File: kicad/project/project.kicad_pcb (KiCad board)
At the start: 2 copper layers, 42 parts, among them J1 SWD, J2 UART, U1 ADS1015, U2 AP7380, U3 STM32L031F4Px, U4 VN7003ALH

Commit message: Placing parts
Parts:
- R1, R2, R7: moved to B.Cu
- moved U1 83.7 mm to (179.1, 102.9), turned to 180 degrees
- moved C6 76.3 mm to (74.9, 60.0)
- moved C4 76.3 mm to (80.7, 52.8)
- moved C5 76.3 mm to (75.3, 58.0)
- moved C7 76.3 mm to (80.7, 54.3)
- moved C8 76.3 mm to (88.3, 45.7)
- moved R11 76.3 mm to (91.7, 48.7)
- moved R12 76.3 mm to (80.7, 55.8)
- moved R13 76.3 mm to (82.0, 57.4)
- moved R16 76.3 mm to (71.7, 58.2)
- moved R3 76.3 mm to (95.0, 45.7)
- moved R4 76.3 mm to (84.0, 52.8)
- moved R5 76.3 mm to (78.6, 58.0)
- moved R6 76.3 mm to (84.0, 54.3)
- moved TP1 76.3 mm to (39.8, 53.4)
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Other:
- board outline added: 70 x 70 mm

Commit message: Panel mount meter
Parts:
- added MES1: Voltmeter, Connector_PinHeader_2.54mm:PinHeader_2x01_P2.54mm_Vertical, F.Cu at (90.1, 79.7)
- added MES2: Amperemeter, Connector_PinHeader_2.54mm:PinHeader_2x01_P2.54mm_Vertical, F.Cu at (97.7, 79.7)
- BT1, D1, D2, D3, D4, SC1: moved to B.Cu
- R1, R2, R7: moved to F.Cu
- U4: footprint theapi:Octapak -> Package_TO_SOT_SMD:Infineon_PG-TO-220-7Lead_TabPin8
- moved U1 82.5 mm to (108.0, 61.0)
- moved D5 81.5 mm to (97.5, 121.0), turned to 270 degrees
- moved BT1 77.4 mm to (97.5, 108.0), turned to 270 degrees
- moved R14 67.1 mm to (104.6, 121.6), turned to 270 degrees
- moved R10 61.1 mm to (107.6, 121.6), turned to 90 degrees
- moved C9 61.0 mm to (107.6, 117.4), turned to 90 degrees
- moved R17 59.0 mm to (108.5, 87.5), turned to 0 degrees
- moved D4 55.4 mm to (108.4, 87.6), turned to 180 degrees
- moved R15 55.1 mm to (110.6, 121.6), turned to 90 degrees
- moved D3 52.6 mm to (108.4, 83.8), turned to 180 degrees
- moved R7 52.6 mm to (108.4, 83.8), turned to 0 degrees
- moved SC1 47.8 mm to (178.0, 113.0), turned to 90 degrees
- moved C11 32.8 mm to (172.5, 116.0)
- moved C1 27.8 mm to (153.1, 116.0), turned to 90 degrees
- moved C10 26.8 mm to (169.5, 116.0)
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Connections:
- BT1 pad 1: /BATT -> Net-(BT1-Pad1)
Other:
- board size 70 x 70 mm -> 95 x 60 mm
- board text added: "CHARGE CONTROLLER"

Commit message: Components placed
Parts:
- removed J2: UART, Connector_PinHeader_2.54mm:PinHeader_1x03_P2.54mm_Vertical
- removed MES1: Voltmeter, Connector_PinHeader_2.54mm:PinHeader_2x01_P2.54mm_Vertical
- removed MES2: Amperemeter, Connector_PinHeader_2.54mm:PinHeader_2x01_P2.54mm_Vertical
- added J3: Voltmeter, Connector_PinHeader_2.54mm:PinHeader_1x02_P2.54mm_Vertical_SMD_Pin1Left, F.Cu at (108.5, 110.0)
- BT1: value Battery -> Battery_Meter; footprint TerminalBlock:TerminalBlock_bornier-2_P5.08mm -> theapi:TerminalBlock_Meter
- D5, U3: moved to B.Cu
- TP1: footprint TestPoint:TestPoint_Pad_2.0x2.0mm -> TestPoint:TestPoint_Pad_D1.0mm
- U4: footprint Package_TO_SOT_SMD:Infineon_PG-TO-220-7Lead_TabPin8 -> theapi:Octapak; moved to B.Cu
- moved TP1 114.9 mm to (122.5, 133.0)
- moved C5 110.7 mm to (163.5, 124.9), turned to 90 degrees
- moved C8 98.9 mm to (144.6, 127.0)
- moved C4 98.3 mm to (137.5, 133.0)
- moved C7 93.7 mm to (138.5, 128.0), turned to 270 degrees
- moved R3 92.7 mm to (144.6, 124.0)
- moved C6 91.8 mm to (136.5, 128.0), turned to 270 degrees
- moved R11 89.2 mm to (130.6, 129.0)
- moved R12 86.1 mm to (130.6, 126.0)
- moved R13 81.7 mm to (130.6, 123.0)
- moved R6 81.5 mm to (108.6, 132.0)
- moved C2 78.8 mm to (122.8, 128.0)
- moved R4 77.2 mm to (108.6, 126.0)
- moved R5 77.0 mm to (108.6, 129.0)
- moved R16 69.1 mm to (123.5, 104.0), turned to 90 degrees
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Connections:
- BT1 pad 1: Net-(BT1-Pad1) -> /BATT
- U3 pad 9: UART_RX -> Net-(U3-Pad9)
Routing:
- net Net-(D5-Pad2): track 0.00 -> 73.4 mm
- net /BATT: track 0.00 -> 20.7 mm
- net +24V: track 0.00 -> 15.5 mm
- net -BATT: track 0.00 -> 6.03 mm
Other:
- board size 95 x 60 mm -> 98 x 60 mm
- board text removed: "CHARGE CONTROLLER"

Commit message: Main power traces
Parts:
- J1: moved to B.Cu
- moved J1 77.9 mm to (107.1, 132.0), turned to 270 degrees
- moved C2 46.0 mm to (168.8, 127.0)
- moved R4 46.0 mm to (154.6, 125.0)
- moved R5 46.0 mm to (154.6, 128.0)
- moved R6 46.0 mm to (154.6, 131.0)
- moved TP1 46.0 mm to (168.5, 132.0)
- moved U1 46.0 mm to (162.5, 127.0)
- moved C1 28.3 mm to (148.8, 119.1)
- moved C3 28.3 mm to (145.8, 119.1)
- moved C4 27.2 mm to (113.6, 120.0)
- moved U2 27.1 mm to (141.5, 122.5), turned to 270 degrees
- moved C6 24.2 mm to (112.5, 125.0)
- moved C7 24.2 mm to (114.5, 125.0)
- moved C8 24.2 mm to (120.6, 124.0)
- moved R11 24.2 mm to (106.6, 126.0)
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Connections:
- net Net-(D5-Pad2) renamed /OUT
- net Net-(R11-Pad1) renamed /INPUT
- R12 pad 1: Net-(R12-Pad1) -> /FR_DIAG
- R12 pad 2: /FR_DIAG -> Net-(R12-Pad2)
- U3 pad 12: /FR_DIAG -> Net-(R12-Pad2)
- U4 pad 6: Net-(R12-Pad1) -> /FR_DIAG
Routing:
- net /OUT: track 73.4 -> 20.8 mm
- net /BATT: track 20.7 -> 0.00 mm
- net -BATT: track 6.03 -> 0.00 mm
- net +24V: track 15.5 -> 14.1 mm, vias 0 -> 27
- added copper zone on B.Cu, net +24V
- added copper zone on F.Cu, net +24V
- added copper zone on B.Cu, net /BATT
- added copper zone on B.Cu, net /OUT

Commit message: Connections
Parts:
- R11, R12, R13: moved to B.Cu
- moved C4 56.1 mm to (169.7, 121.7)
- moved C6 56.1 mm to (168.6, 126.7)
- moved C7 56.1 mm to (170.6, 126.7)
- moved C8 56.1 mm to (176.7, 125.7)
- moved R3 56.1 mm to (176.7, 122.7)
- moved U3 56.1 mm to (169.6, 125.7)
- moved C2 54.7 mm to (114.0, 127.3), turned to 180 degrees
- moved TP1 49.3 mm to (119.4, 127.5)
- moved U1 48.5 mm to (114.1, 123.4)
- moved J1 42.4 mm to (149.5, 131.0)
- moved R6 37.7 mm to (118.8, 119.4), turned to 270 degrees
- moved R5 34.0 mm to (121.8, 119.4), turned to 270 degrees
- moved R11 31.1 mm to (137.7, 127.7)
- moved R12 31.1 mm to (137.7, 124.7)
- moved R13 31.1 mm to (137.7, 121.7)
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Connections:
- net /LED renamed /LED_1
- net /OUT renamed /LED_4
- net /PA4 renamed /LED_3
- net Net-(R2-Pad2) renamed /LED_2
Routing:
- net +3V3: track 0.00 -> 121.6 mm, vias 0 -> 2
- net /BATT_SENSE: track 0.00 -> 111.9 mm, vias 0 -> 1
- net /LED_3: track 0.00 -> 110.7 mm, vias 0 -> 1
- net /PANEL_SENSE: track 0.00 -> 102.7 mm, vias 0 -> 1
- net ADC_RDY: track 0.00 -> 68.4 mm, vias 0 -> 3
- net SDA: track 0.00 -> 64.2 mm, vias 0 -> 4
- net SCL: track 0.00 -> 62.8 mm, vias 0 -> 3
- net /LED_2: track 0.00 -> 59.9 mm, vias 0 -> 1
- net CURRENT_SENSE: track 0.00 -> 56.0 mm, vias 0 -> 1
- net +24V: track 14.1 -> 67.3 mm
- net /LED_1: track 0.00 -> 49.4 mm, vias 0 -> 1
- net GND: track 0.00 -> 46.8 mm, vias 0 -> 1
- net /FR_DIAG: track 0.00 -> 32.1 mm, vias 0 -> 2
- net Net-(R12-Pad2): track 0.00 -> 29.4 mm
- net /PWM: track 0.00 -> 28.4 mm
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- added copper zone on B.Cu, net -BATT

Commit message: Connected
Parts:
- moved C4 0.28 mm to (169.7, 121.4)
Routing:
- net GND: track 46.8 -> 326.9 mm, vias 1 -> 11
- net +24V: track 67.3 -> 127.6 mm
- net /BATT_SENSE: track 111.9 -> 121.8 mm
- net /AIN3: track 0.00 -> 7.53 mm
- net /PANEL_SENSE: track 102.7 -> 96.1 mm
- net /FR_DIAG: track 32.1 -> 34.7 mm
- net +3V3: track 121.6 -> 121.0 mm
- net CURRENT_SENSE: track 56.0 -> 56.6 mm
- added copper zone on B.Cu, net GND
- added copper zone on F.Cu, net GND

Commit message: Connected
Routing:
- net GND: track 326.9 -> 335.6 mm
- net +24V: track 127.6 -> 134.2 mm
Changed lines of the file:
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@@
     (thickness 1.6)
     (drawings 24)
-    (tracks 426)
+    (tracks 431)
     (zones 0)
     (modules 42)
@@
   (segment (start 135.1 126.4) (end 133.5 128) (width 0.25) (layer F.Cu) (net 2))
   (segment (start 135.1 122.85) (end 135.1 126.4) (width 0.25) (layer F.Cu) (net 2))
-  (segment (start 92.5 97.75) (end 100.69 105.94) (width 0.25) (layer F.Cu) (net 2))
-  (segment (start 92.5 96) (end 92.5 97.75) (width 0.25) (layer F.Cu) (net 2))
-  (segment (start 100.69 108.575002) (end 104.284998 112.17) (width 0.25) (layer F.Cu) (net 2))
-  (segment (start 100.69 105.94) (end 100.69 108.575002) (width 0.25) (layer F.Cu) (net 2))
-  (segment (start 104.284998 112.17) (end 115.76 112.17) (width 0.25) (layer F.Cu) (net 2))
-  (segment (start 122.18 105.75) (end 132.75 105.75) (width 0.25) (layer F.Cu) (net 2))
-  (segment (start 115.76 112.17) (end 122.18 105.75) (width 0.25) (layer F.Cu) (net 2))
   (via (at 151.5 120.75) (size 0.8) (drill 0.4) (layers F.Cu B.Cu) (net 2))
   (segment (start 151.5 120.75) (end 150.35 120.75) (width 0.25) (layer B.Cu) (net 2))
@@
   (segment (start 143 125.5) (end 141.55 125.5) (width 0.25) (layer F.Cu) (net 2))
   (via (at 150 123) (size 0.8) (drill 0.4) (layers F.Cu B.Cu) (net 2))
+  (segment (start 122.18 105.75) (end 132.75 105.75) (width 0.25) (layer F.Cu) (net 2))
+  (segment (start 121.5 106.43) (end 122.18 105.75) (width 0.25) (layer F.Cu) (net 2))
+  (segment (start 104.5 115.5) (end 119.5 115.5) (width 0.25) (layer F.Cu) (net 2))
+  (segment (start 92.5 96) (end 92.5 97.75) (width 0.25) (layer F.Cu) (net 2))
+  (segment (start 119.5 115.5) (end 121.5 113.5) (width 0.25) (layer F.Cu) (net 2))
+  (segment (start 92.5 97.75) (end 100.69 105.94) (width 0.25) (layer F.Cu) (net 2))
+  (segment (start 121.5 113.5) (end 121.5 106.43) (width 0.25) (layer F.Cu) (net 2))
+  (segment (start 100.69 105.94) (end 100.69 111.69) (width 0.25) (layer F.Cu) (net 2))
+  (segment (start 100.69 111.69) (end 104.5 115.5) (width 0.25) (layer F.Cu) (net 2))
   (via (at 141.3 113.6) (size 0.8) (drill 0.4) (layers F.Cu B.Cu) (net 3))
   (via (at 141.3 111.2) (size 0.8) (drill 0.4) (layers F.Cu B.Cu) (net 3))
@@
   (segment (start 176.5 113.13) (end 176.08 113.55) (width 0.25) (layer F.Cu) (net 3))
   (segment (start 176.5 108) (end 176.5 113.13) (width 0.25) (layer F.Cu) (net 3))
-  (segment (start 133.61 103.61) (end 137.5 107.5) (width 0.25) (layer F.Cu) (net 3))
-  (segment (start 107.77 108.57) (end 110.01 110.81) (width 0.25) (layer F.Cu) (net 3))
-  (segment (start 107.77 96.345) (end 107.77 108.57) (width 0.25) (layer F.Cu) (net 3))
-  (segment (start 110.01 110.81) (end 115.81 110.81) (width 0.25) (layer F.Cu) (net 3))
-  (segment (start 123.01 103.61) (end 133.61 103.61) (width 0.25) (layer F.Cu) (net 3))
-  (segment (start 115.81 110.81) (end 123.01 103.61) (width 0.25) (layer F.Cu) (net 3))
   (segment (start 144.875 108) (end 140.875 112) (width 0.25) (layer B.Cu) (net 3))
   (segment (start 176.5 108) (end 144.875 108) (width 0.25) (layer B.Cu) (net 3))
@@
   (segment (start 145.75 118.25) (end 145.75 115.75) (width 0.25) (layer F.Cu) (net 3))
   (segment (start 148.85 118.25) (end 145.75 118.25) (width 0.25) (layer F.Cu) (net 3))
+  (segment (start 135 105) (end 137.5 107.5) (width 0.25) (layer F.Cu) (net 3))
+  (segment (start 121.62 105) (end 135 105) (width 0.25) (layer F.Cu) (net 3))
+  (segment (start 107.77 96.345) (end 107.77 110.27) (width 0.25) (layer F.Cu) (net 3))
+  (segment (start 120.5 112.5) (end 120.5 106.12) (width 0.25) (layer F.Cu) (net 3))
+  (segment (start 112 114.5) (end 118.5 114.5) (width 0.25) (layer F.Cu) (net 3))
+  (segment (start 107.77 110.27) (end 112 114.5) (width 0.25) (layer F.Cu) (net 3))
+  (segment (start 120.5 106.12) (end 121.62 105) (width 0.25) (layer F.Cu) (net 3))
+  (segment (start 118.5 114.5) (end 120.5 112.5) (width 0.25) (layer F.Cu) (net 3))
   (segment (start 170.6 125.825) (end 170.6 123.900002) (width 0.25) (layer F.Cu) (net 4))
   (segment (start 170.6 124.4) (end 170.6 123.900002) (width 0.25) (layer B.Cu) (net 4))
@@
   (segment (start 141.849991 127.949991) (end 139.099072 125.199072) (width 0.25) (layer B.Cu) (net 30))
   (segment (start 113.66 106.020102) (end 113.66 108) (width 0.25) (layer F.Cu) (net 31))
-  (segment (start 107.6 89.1) (end 113.66 95.16) (width 0.25) (layer F.Cu) (net 31))
-  (segment (start 113.66 95.16) (end 113.66 106.020102) (width 0.25) (layer F.Cu) (net 31))
   (segment (start 101.175 89.1) (end 107.6 89.1) (width 0.25) (layer F.Cu) (net 31))
+  (segment (start 110 102.360102) (end 113.66 106.020102) (width 0.25) (layer F.Cu) (net 31))
+  (segment (start 107.6 89.1) (end 110 91.5) (width 0.25) (layer F.Cu) (net 31))
+  (segment (start 110 91.5) (end 110 102.360102) (width 0.25) (layer F.Cu) (net 31))
   (via (at 177.8 90.6) (size 0.8) (drill 0.4) (layers F.Cu B.Cu) (net 32))
   (segment (start 175.245 90.6) (end 175.235 90.59) (width 0.25) (layer F.Cu) (net 32))
@@
     (polygon
       (pts
-        (xy 134.1 112.8) (xy 129.3 112.8) (xy 127.5 112.8) (xy 115.3 103.2) (xy 111.1 103.2)
+        (xy 134.1 112.8) (xy 129.3 112.8) (xy 127.5 112.8) (xy 115 105) (xy 111.1 103.2)
         (xy 111.1 113) (xy 115.3 113) (xy 127.7 116.4) (xy 134.1 116.4)
       )
@@
     (polygon
       (pts
-        (xy 111.1 103.2) (xy 115.3 103.2) (xy 127.5 112.8) (xy 129.3 112.8) (xy 134.1 112.8)
+        (xy 111.1 103.2) (xy 115 105) (xy 127.5 112.8) (xy 129.3 112.8) (xy 134.1 112.8)
         (xy 134.1 116.4) (xy 127.7 116.4) (xy 115.3 113) (xy 111.1 113)
       )
@@
     (polygon
       (pts
-        (xy 186.5 98) (xy 186.5 120) (xy 179.5 120) (xy 179.5 104.5) (xy 118.5 104.5)
-        (xy 114.5 102) (xy 95.5 102) (xy 95.5 97) (xy 114.5 97) (xy 186.5 97)
+        (xy 186.5 98) (xy 186.5 120) (xy 179.5 120) (xy 179.5 104.5) (xy 117 104.5)
+        (xy 111 102) (xy 95.5 102) (xy 95.5 97) (xy 114.5 97) (xy 186.5 97)
       )
     )
@@
     (polygon
       (pts
-        (xy 134.55 104.45) (xy 134.55 108.45) (xy 124.05 108.65) (xy 119.25 104.75)
+        (xy 134.55 104.45) (xy 134.55 108.45) (xy 124.05 108.65) (xy 111 102)
       )
     )

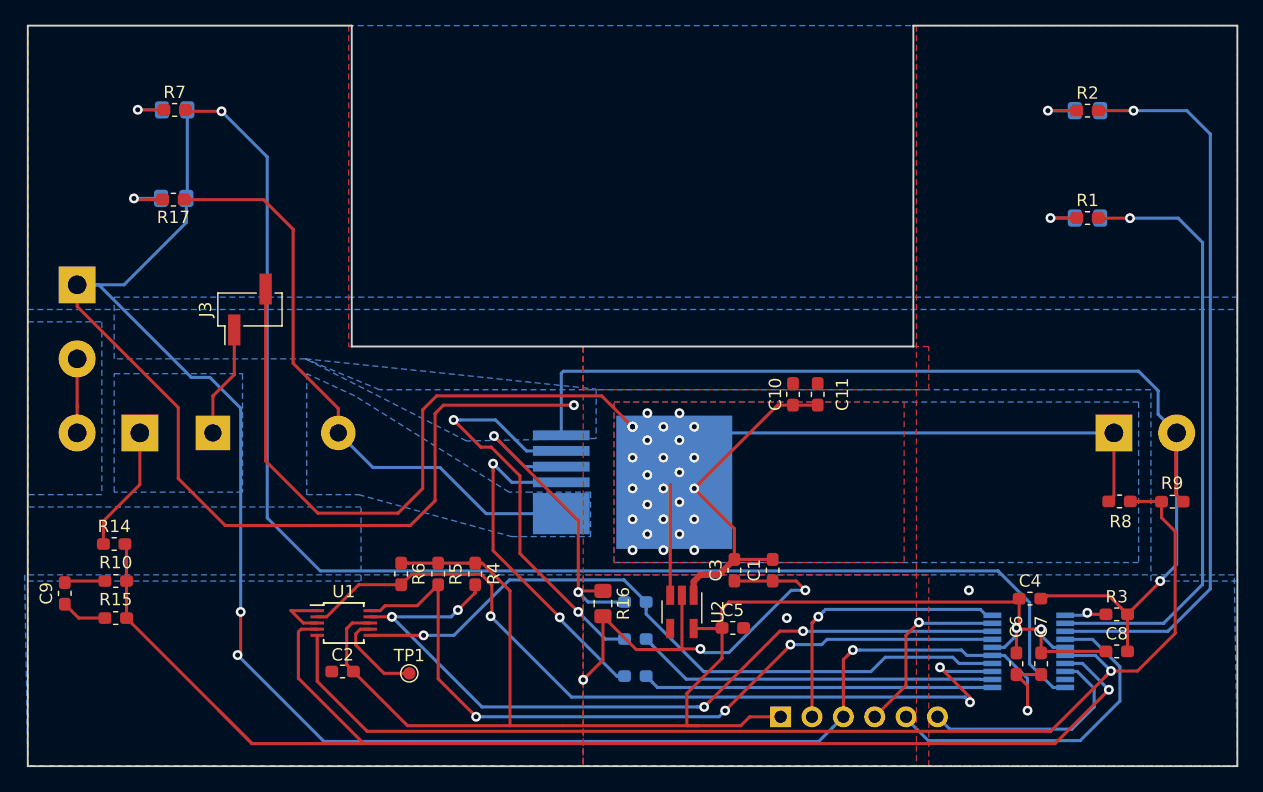
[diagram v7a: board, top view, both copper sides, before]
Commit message: Avoid power fills
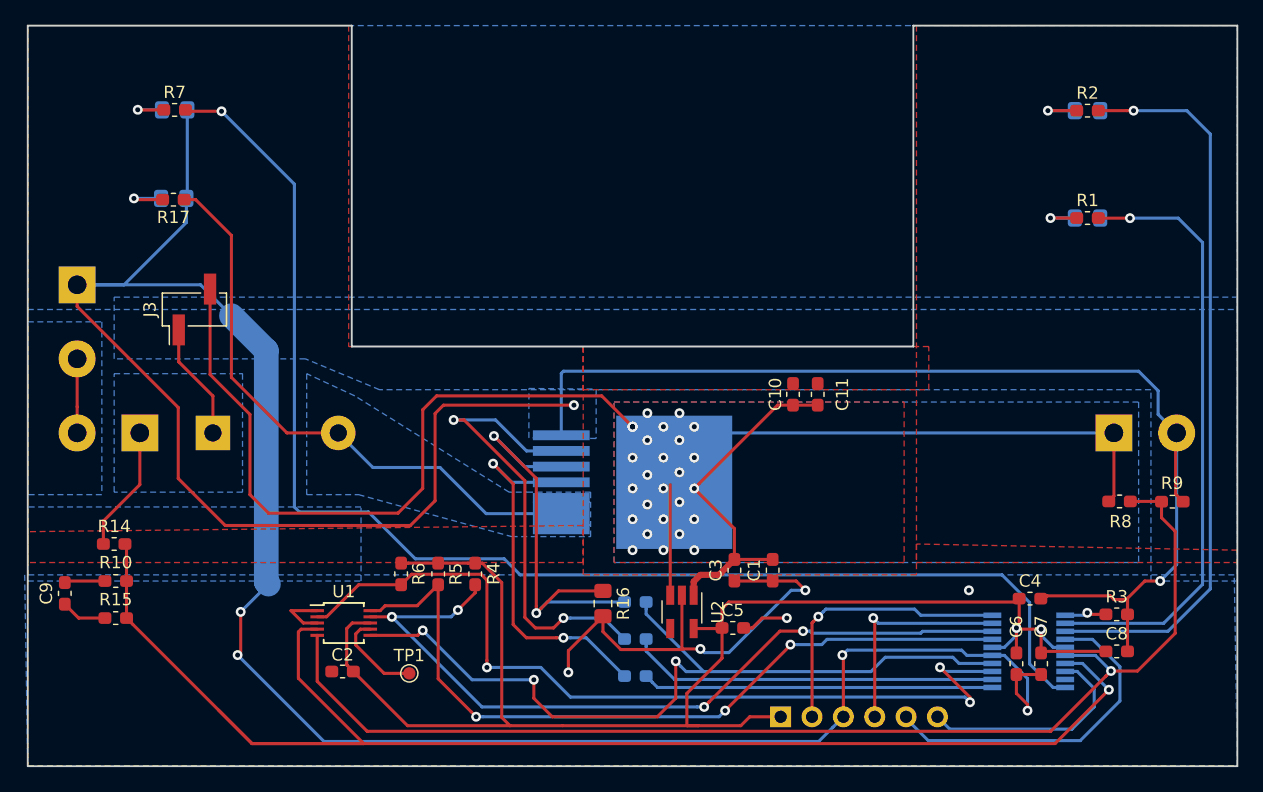
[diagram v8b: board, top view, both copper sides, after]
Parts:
- moved J3 4.50 mm to (102.0, 98.0)
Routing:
- net GND: track 335.6 -> 347.6 mm
- net CURRENT_SENSE: track 56.6 -> 66.6 mm, vias 1 -> 3
- net Net-(R13-Pad1): track 28.1 -> 35.9 mm
- net +24V: track 134.2 -> 138.4 mm
- net /FR_DIAG: track 34.7 -> 38.1 mm
- net SWDI0: track 15.1 -> 17.9 mm
- net ADC_RDY: track 68.4 -> 71.0 mm
- net /INPUT: track 28.1 -> 30.6 mm
- net /LED_3: track 110.7 -> 108.9 mm
- net /LED_4: track 48.6 -> 47.8 mm
- net Net-(R12-Pad2): track 29.4 -> 30.0 mm
